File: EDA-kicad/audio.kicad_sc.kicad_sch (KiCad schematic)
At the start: 8 parts, among them J1 SJ2-35894B-SMT-TR, U7 CODEC-TLV320AIC3204IRHBR

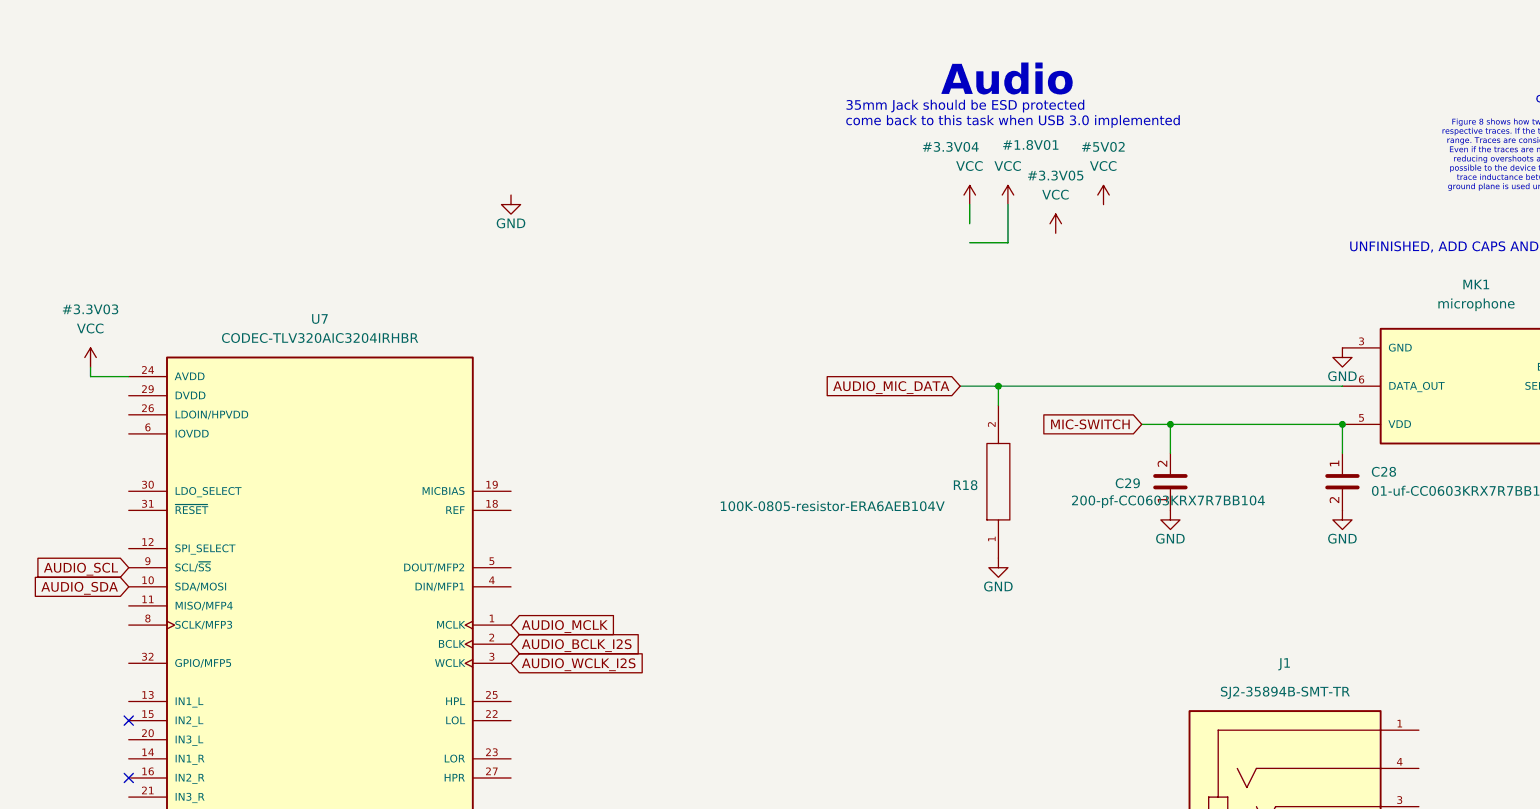
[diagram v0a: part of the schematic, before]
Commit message: reannotate entire schematic
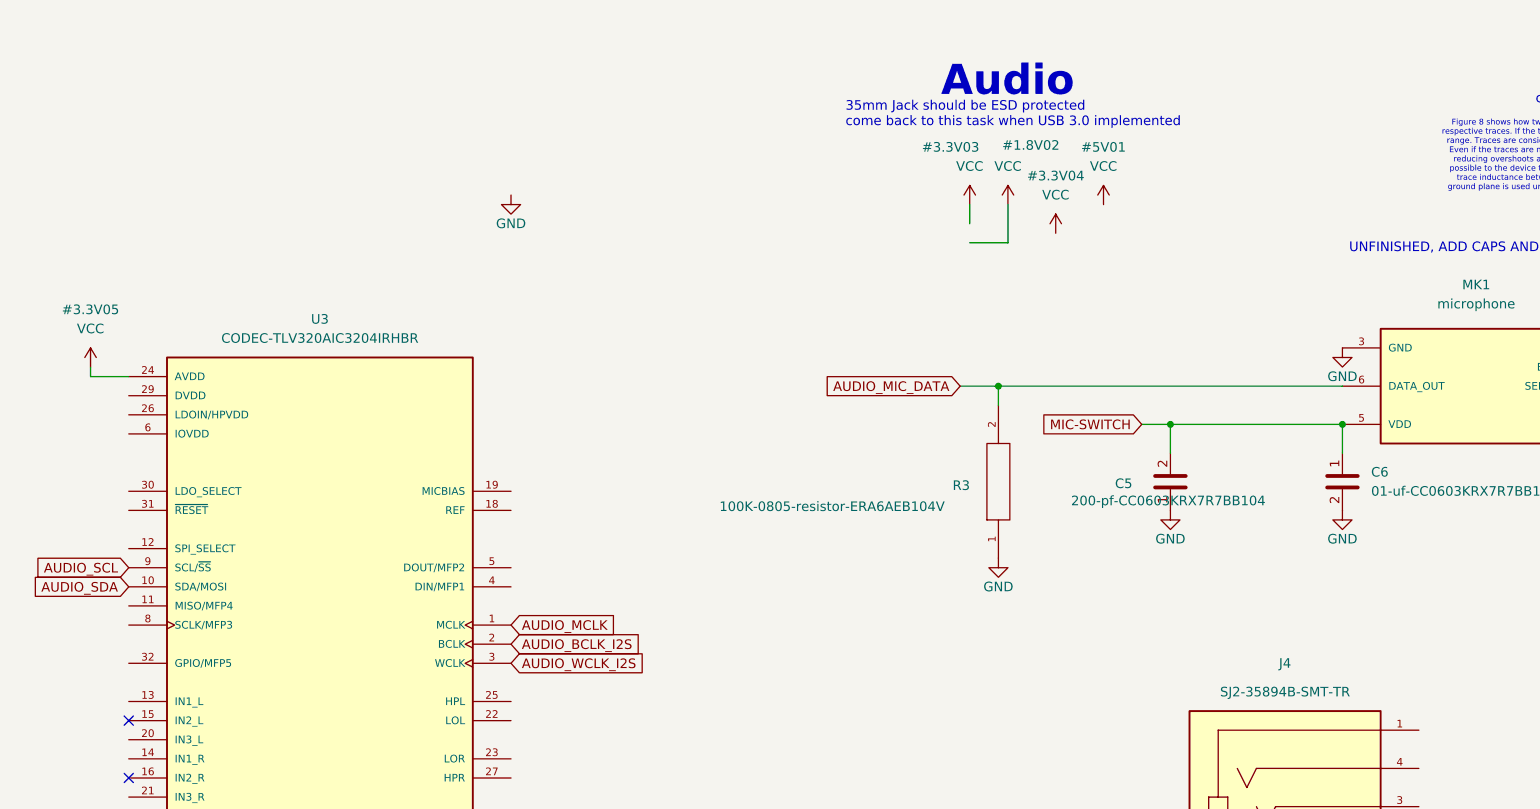
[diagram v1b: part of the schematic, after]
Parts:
- renumbered C29 to C5, C28 to C6, J1 to J4, R18 to R3, U7 to U3
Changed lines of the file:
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@@
 		(on_board yes)
 		(dnp no)
-		(property "Reference" "#PWR0105"
+		(property "Reference" "#PWR070"
 			(at 195.58 83.82 0)
 			(effects
@@
 			(project "cm5-carrier"
 				(path "/28c5e4fe-1ec7-4477-97f0-d2ec1401fad5/dae24383-d996-4b63-b3a8-c19902a00c63"
-					(reference "#PWR0105")
+					(reference "#PWR070")
 					(unit 1)
 				)
@@
 		(on_board yes)
 		(dnp no)
-		(property "Reference" "C28"
+		(property "Reference" "C6"
 			(at 199.39 72.3899 90)
 			(effects
@@
 			(project ""
 				(path "/28c5e4fe-1ec7-4477-97f0-d2ec1401fad5/dae24383-d996-4b63-b3a8-c19902a00c63"
-					(reference "C28")
+					(reference "C6")
 					(unit 1)
 				)
@@
 		(on_board yes)
 		(dnp no)
-		(property "Reference" "#1.8V01"
+		(property "Reference" "#1.8V02"
 			(at 154.178 28.956 0)
 			(effects
@@
 			(project "cm5-carrier"
 				(path "/28c5e4fe-1ec7-4477-97f0-d2ec1401fad5/dae24383-d996-4b63-b3a8-c19902a00c63"
-					(reference "#1.8V01")
+					(reference "#1.8V02")
 					(unit 1)
 				)
@@
 		(on_board yes)
 		(dnp no)
-		(property "Reference" "#PWR077"
+		(property "Reference" "#PWR068"
 			(at 255.27 67.31 0)
 			(effects
@@
 			(project "cm5-carrier"
 				(path "/28c5e4fe-1ec7-4477-97f0-d2ec1401fad5/dae24383-d996-4b63-b3a8-c19902a00c63"
-					(reference "#PWR077")
+					(reference "#PWR068")
 					(unit 1)
 				)
@@
 		(on_board yes)
 		(dnp no)
-		(property "Reference" "#PWR0106"
+		(property "Reference" "#PWR069"
 			(at 172.72 83.82 0)
 			(effects
@@
 			(project "cm5-carrier"
 				(path "/28c5e4fe-1ec7-4477-97f0-d2ec1401fad5/dae24383-d996-4b63-b3a8-c19902a00c63"
-					(reference "#PWR0106")
+					(reference "#PWR069")
 					(unit 1)
 				)
@@
 		(on_board yes)
 		(dnp no)
-		(property "Reference" "#3.3V05"
+		(property "Reference" "#3.3V04"
 			(at 157.48 33.02 0)
 			(effects
@@
 			(project "cm5-carrier"
 				(path "/28c5e4fe-1ec7-4477-97f0-d2ec1401fad5/dae24383-d996-4b63-b3a8-c19902a00c63"
-					(reference "#3.3V05")
+					(reference "#3.3V04")
 					(unit 1)
 				)
@@
 		(on_board yes)
 		(dnp no)
-		(property "Reference" "#PWR041"
+		(property "Reference" "#PWR066"
 			(at 85.09 41.91 0)
 			(effects
@@
 			(project "cm5-carrier"
 				(path "/28c5e4fe-1ec7-4477-97f0-d2ec1401fad5/dae24383-d996-4b63-b3a8-c19902a00c63"
-					(reference "#PWR041")
+					(reference "#PWR066")
 					(unit 1)
 				)
@@
 		(on_board yes)
 		(dnp no)
-		(property "Reference" "C29"
+		(property "Reference" "C5"
 			(at 165.354 73.914 90)
 			(effects
@@
 			(project ""
 				(path "/28c5e4fe-1ec7-4477-97f0-d2ec1401fad5/dae24383-d996-4b63-b3a8-c19902a00c63"
-					(reference "C29")
+					(reference "C5")
 					(unit 1)
 				)
@@
 		(on_board yes)
 		(dnp no)
-		(property "Reference" "#PWR059"
+		(property "Reference" "#PWR067"
 			(at 195.58 62.23 0)
 			(effects
@@
 			(project "cm5-carrier"
 				(path "/28c5e4fe-1ec7-4477-97f0-d2ec1401fad5/dae24383-d996-4b63-b3a8-c19902a00c63"
-					(reference "#PWR059")
+					(reference "#PWR067")
 					(unit 1)
 				)
@@
 		(on_board yes)
 		(dnp no)
-		(property "Reference" "#PWR0104"
+		(property "Reference" "#PWR071"
 			(at 149.86 90.17 0)
 			(effects
@@
 			(project "cm5-carrier"
 				(path "/28c5e4fe-1ec7-4477-97f0-d2ec1401fad5/dae24383-d996-4b63-b3a8-c19902a00c63"
-					(reference "#PWR0104")
+					(reference "#PWR071")
 					(unit 1)
 				)
@@
 		(on_board yes)
 		(dnp no)
-		(property "Reference" "#5V02"
+		(property "Reference" "#5V01"
 			(at 163.83 29.21 0)
 			(effects
@@
 			(project "cm5-carrier"
 				(path "/28c5e4fe-1ec7-4477-97f0-d2ec1401fad5/dae24383-d996-4b63-b3a8-c19902a00c63"
-					(reference "#5V02")
+					(reference "#5V01")
 					(unit 1)
 				)
@@
 		(on_board yes)
 		(dnp no)
-		(property "Reference" "R18"
+		(property "Reference" "R3"
 			(at 143.764 74.168 90)
 			(effects
@@
 			(project ""
 				(path "/28c5e4fe-1ec7-4477-97f0-d2ec1401fad5/dae24383-d996-4b63-b3a8-c19902a00c63"
-					(reference "R18")
+					(reference "R3")
 					(unit 1)
 				)
@@
 		(on_board yes)
 		(dnp no)
-		(property "Reference" "#3.3V04"
+		(property "Reference" "#3.3V03"
 			(at 143.51 29.21 0)
 			(effects
@@
 			(project "cm5-carrier"
 				(path "/28c5e4fe-1ec7-4477-97f0-d2ec1401fad5/dae24383-d996-4b63-b3a8-c19902a00c63"
-					(reference "#3.3V04")
+					(reference "#3.3V03")
 					(unit 1)
 				)
@@
 		(on_board yes)
 		(dnp no)
-		(property "Reference" "J1"
+		(property "Reference" "J4"
 			(at 187.96 97.79 0)
 			(effects
@@
 			(project "cm5-carrier"
 				(path "/28c5e4fe-1ec7-4477-97f0-d2ec1401fad5/dae24383-d996-4b63-b3a8-c19902a00c63"
-					(reference "J1")
+					(reference "J4")
 					(unit 1)
 				)
@@
 		(on_board yes)
 		(dnp no)
-		(property "Reference" "#3.3V03"
+		(property "Reference" "#3.3V05"
 			(at 29.21 50.8 0)
 			(effects
@@
 			(project "cm5-carrier"
 				(path "/28c5e4fe-1ec7-4477-97f0-d2ec1401fad5/dae24383-d996-4b63-b3a8-c19902a00c63"
-					(reference "#3.3V03")
+					(reference "#3.3V05")
 					(unit 1)
 				)
@@
 		(dnp no)
 		(fields_autoplaced yes)
-		(property "Reference" "U7"
+		(property "Reference" "U3"
 			(at 59.69 52.07 0)
 			(effects
@@
 			(project "cm5-carrier"
 				(path "/28c5e4fe-1ec7-4477-97f0-d2ec1401fad5/dae24383-d996-4b63-b3a8-c19902a00c63"
-					(reference "U7")
+					(reference "U3")
 					(unit 1)
 				)
@@
 		(dnp no)
 		(fields_autoplaced yes)
-		(property "Reference" "#PWR042"
+		(property "Reference" "#PWR072"
 			(at 88.9 142.24 0)
 			(effects
@@
 			(project "cm5-carrier"
 				(path "/28c5e4fe-1ec7-4477-97f0-d2ec1401fad5/dae24383-d996-4b63-b3a8-c19902a00c63"
-					(reference "#PWR042")
-					(unit 1)
-				)
+					(reference "#PWR072")
+					(unit 1)
+				)

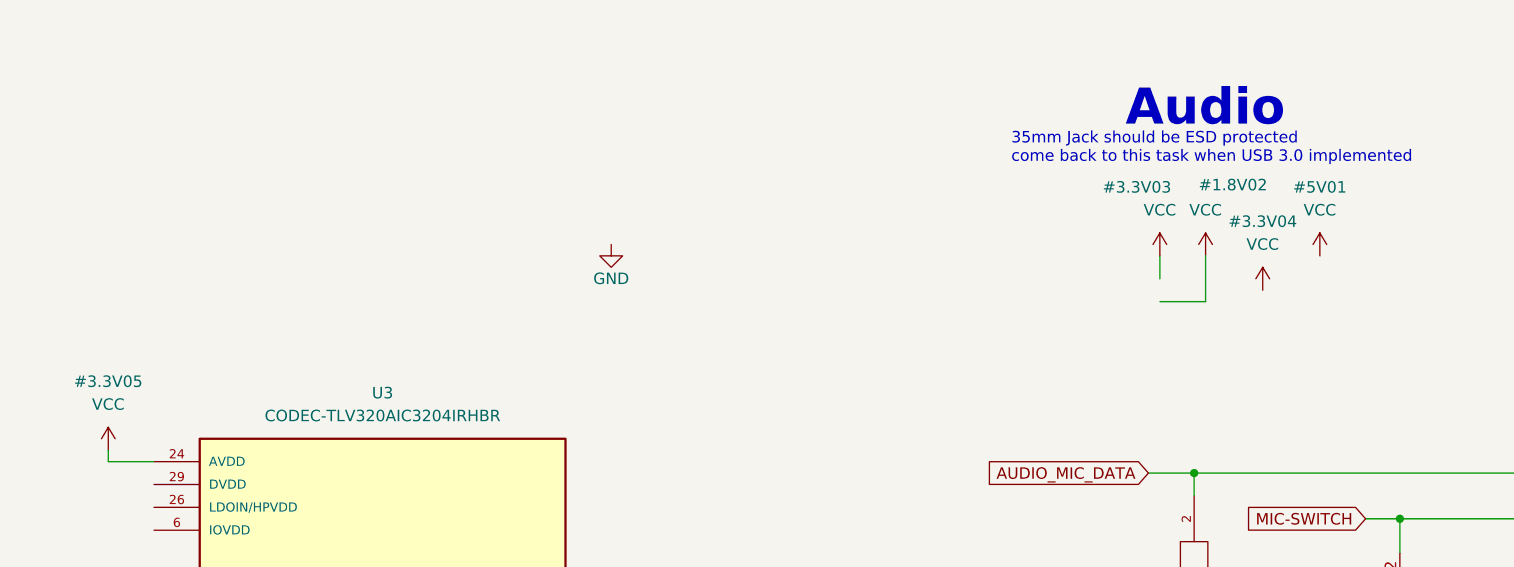
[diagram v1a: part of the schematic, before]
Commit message: add new switches and reannotate
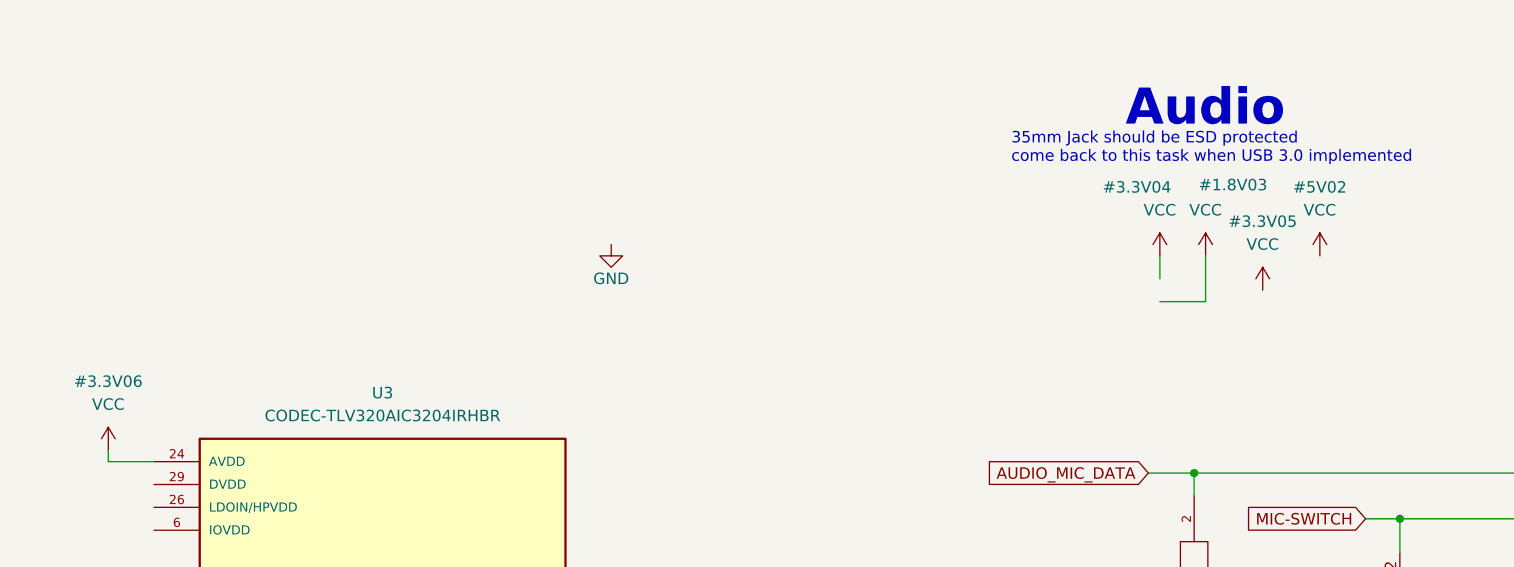
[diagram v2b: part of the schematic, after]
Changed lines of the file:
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@@
 		(on_board yes)
 		(dnp no)
-		(property "Reference" "#1.8V02"
+		(property "Reference" "#1.8V03"
 			(at 154.178 28.956 0)
 			(effects
@@
 			(project "cm5-carrier"
 				(path "/28c5e4fe-1ec7-4477-97f0-d2ec1401fad5/dae24383-d996-4b63-b3a8-c19902a00c63"
-					(reference "#1.8V02")
+					(reference "#1.8V03")
 					(unit 1)
 				)
@@
 		(on_board yes)
 		(dnp no)
-		(property "Reference" "#3.3V04"
+		(property "Reference" "#3.3V05"
 			(at 157.48 33.02 0)
 			(effects
@@
 			(project "cm5-carrier"
 				(path "/28c5e4fe-1ec7-4477-97f0-d2ec1401fad5/dae24383-d996-4b63-b3a8-c19902a00c63"
-					(reference "#3.3V04")
+					(reference "#3.3V05")
 					(unit 1)
 				)
@@
 		(on_board yes)
 		(dnp no)
-		(property "Reference" "#5V01"
+		(property "Reference" "#5V02"
 			(at 163.83 29.21 0)
 			(effects
@@
 			(project "cm5-carrier"
 				(path "/28c5e4fe-1ec7-4477-97f0-d2ec1401fad5/dae24383-d996-4b63-b3a8-c19902a00c63"
-					(reference "#5V01")
+					(reference "#5V02")
 					(unit 1)
 				)
@@
 		(on_board yes)
 		(dnp no)
-		(property "Reference" "#3.3V03"
+		(property "Reference" "#3.3V04"
 			(at 143.51 29.21 0)
 			(effects
@@
 			(project "cm5-carrier"
 				(path "/28c5e4fe-1ec7-4477-97f0-d2ec1401fad5/dae24383-d996-4b63-b3a8-c19902a00c63"
-					(reference "#3.3V03")
+					(reference "#3.3V04")
 					(unit 1)
 				)
@@
 		(on_board yes)
 		(dnp no)
-		(property "Reference" "#3.3V05"
+		(property "Reference" "#3.3V06"
 			(at 29.21 50.8 0)
 			(effects
@@
 			(project "cm5-carrier"
 				(path "/28c5e4fe-1ec7-4477-97f0-d2ec1401fad5/dae24383-d996-4b63-b3a8-c19902a00c63"
-					(reference "#3.3V05")
-					(unit 1)
-				)
+					(reference "#3.3V06")
+					(unit 1)
+				)

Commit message: assign power section footprints and import to pcb
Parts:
- C6: footprint CC0603KRX7R7BB104:CAPC1608X90 -> SPIRIT-footprints:0603-capacitor
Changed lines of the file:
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@@
 			)
 		)
-		(property "Footprint" "CC0603KRX7R7BB104:CAPC1608X90"
+		(property "Footprint" "SPIRIT-footprints:0603-capacitor"
 			(at 195.58 73.66 0)
 			(effects

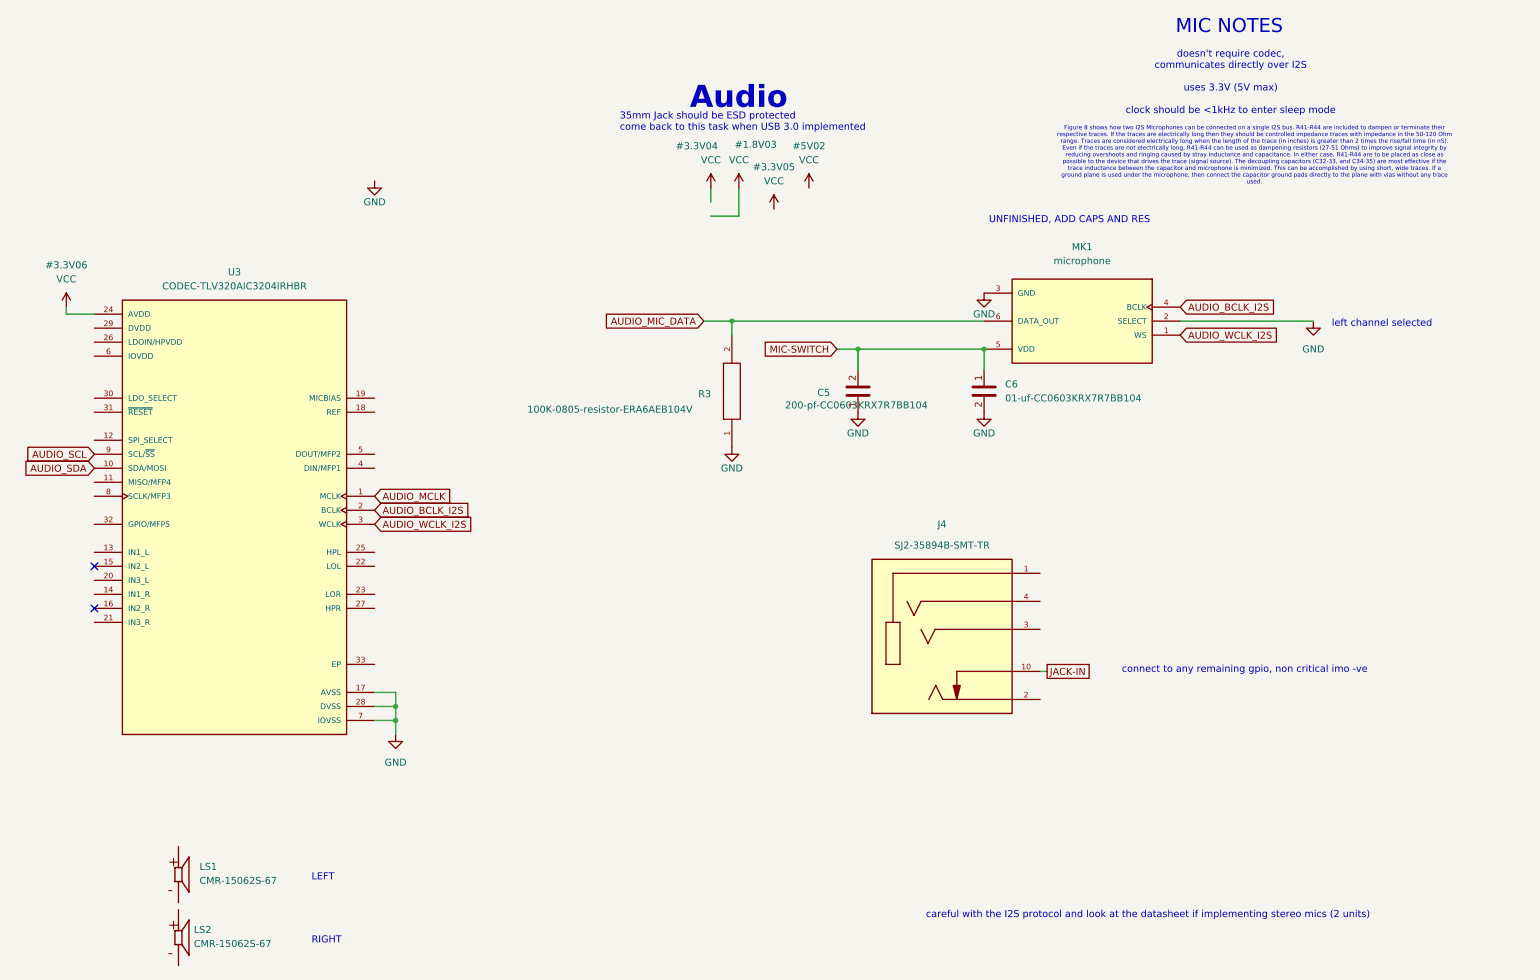
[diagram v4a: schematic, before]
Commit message: set everything except from power to DNP
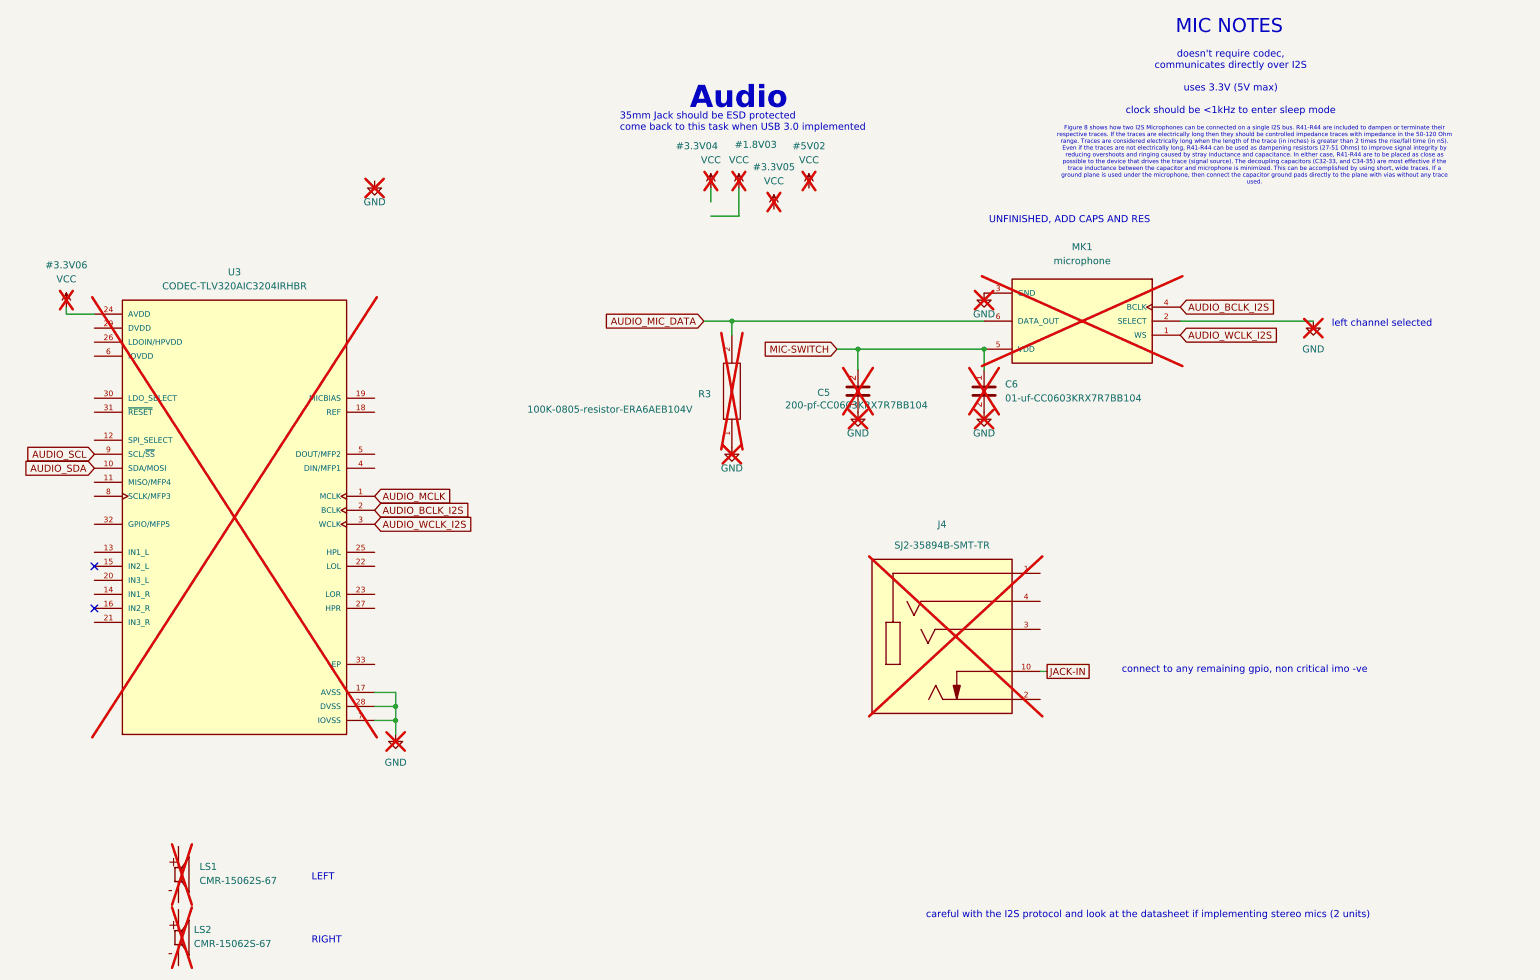
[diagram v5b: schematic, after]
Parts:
- C5, C6, J4, LS1, LS2, MK1, R3, U3: now not fitted
